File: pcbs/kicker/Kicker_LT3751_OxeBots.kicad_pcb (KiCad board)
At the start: 2 copper layers, 117.9 x 140 mm, 127 parts, among them J1 XT30PW-F, J2 12V, J3 3.3V, J4 I2C, J5 ST Link, J6 XT30PW-F, Q1 IRFB4227, Q2 BSS138, Q3 BSS138, Q4 FQPF20N60, SW1 SW_Push, T1 DCT15EFD-U44S003, U1 STM32G031F6Px, U2 LT3751, U3 TLV9002, U4 AQV454, U5 HCNR201, U6 HCPL-3120, U7 LM358

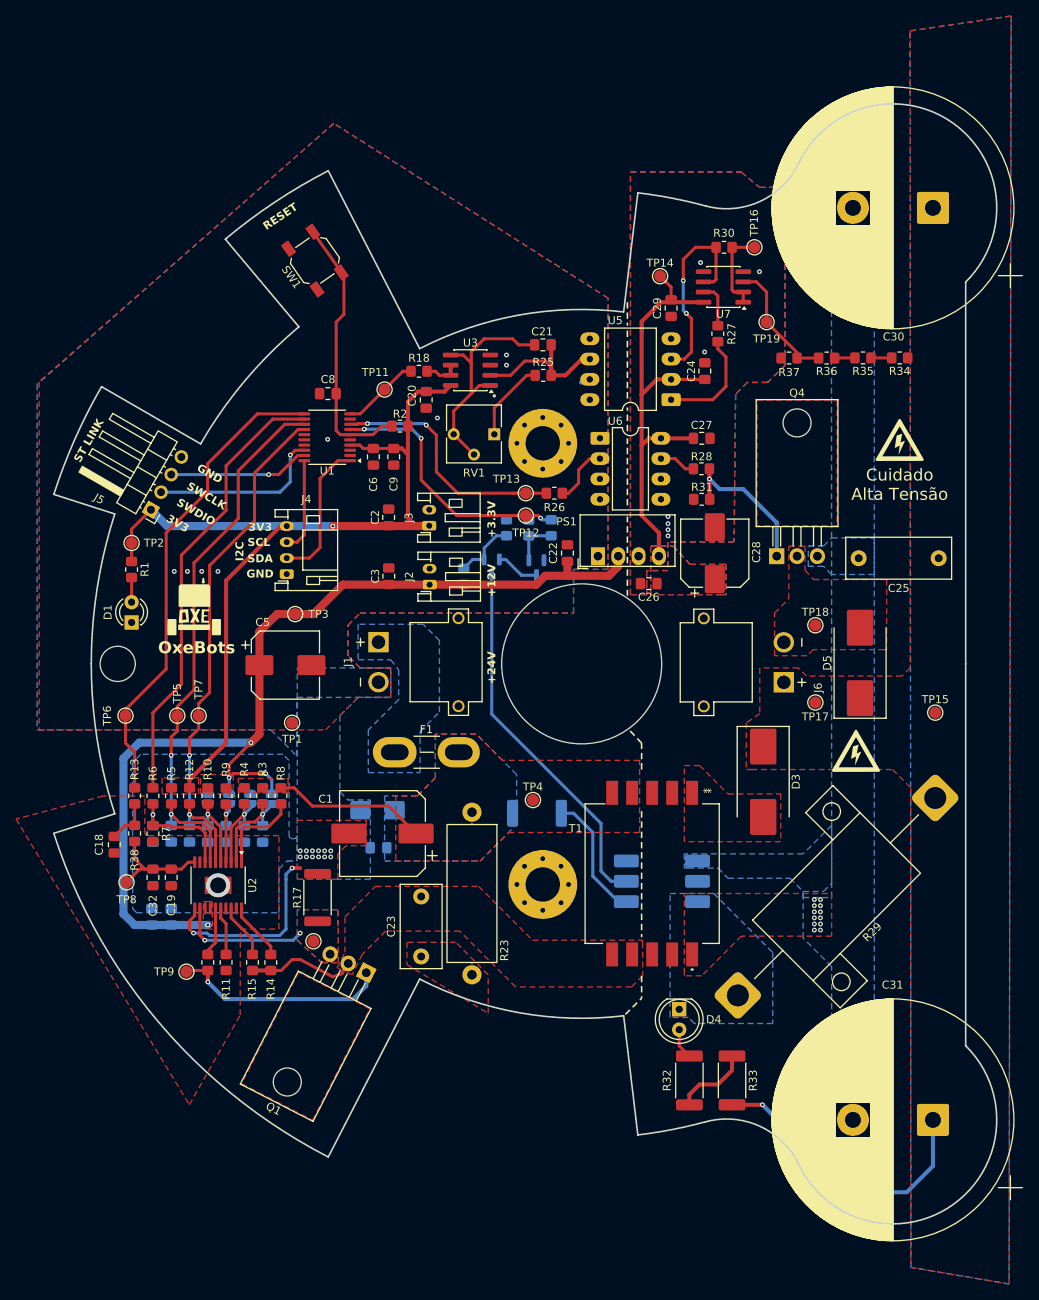
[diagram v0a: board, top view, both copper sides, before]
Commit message: Updated to IDC Connector
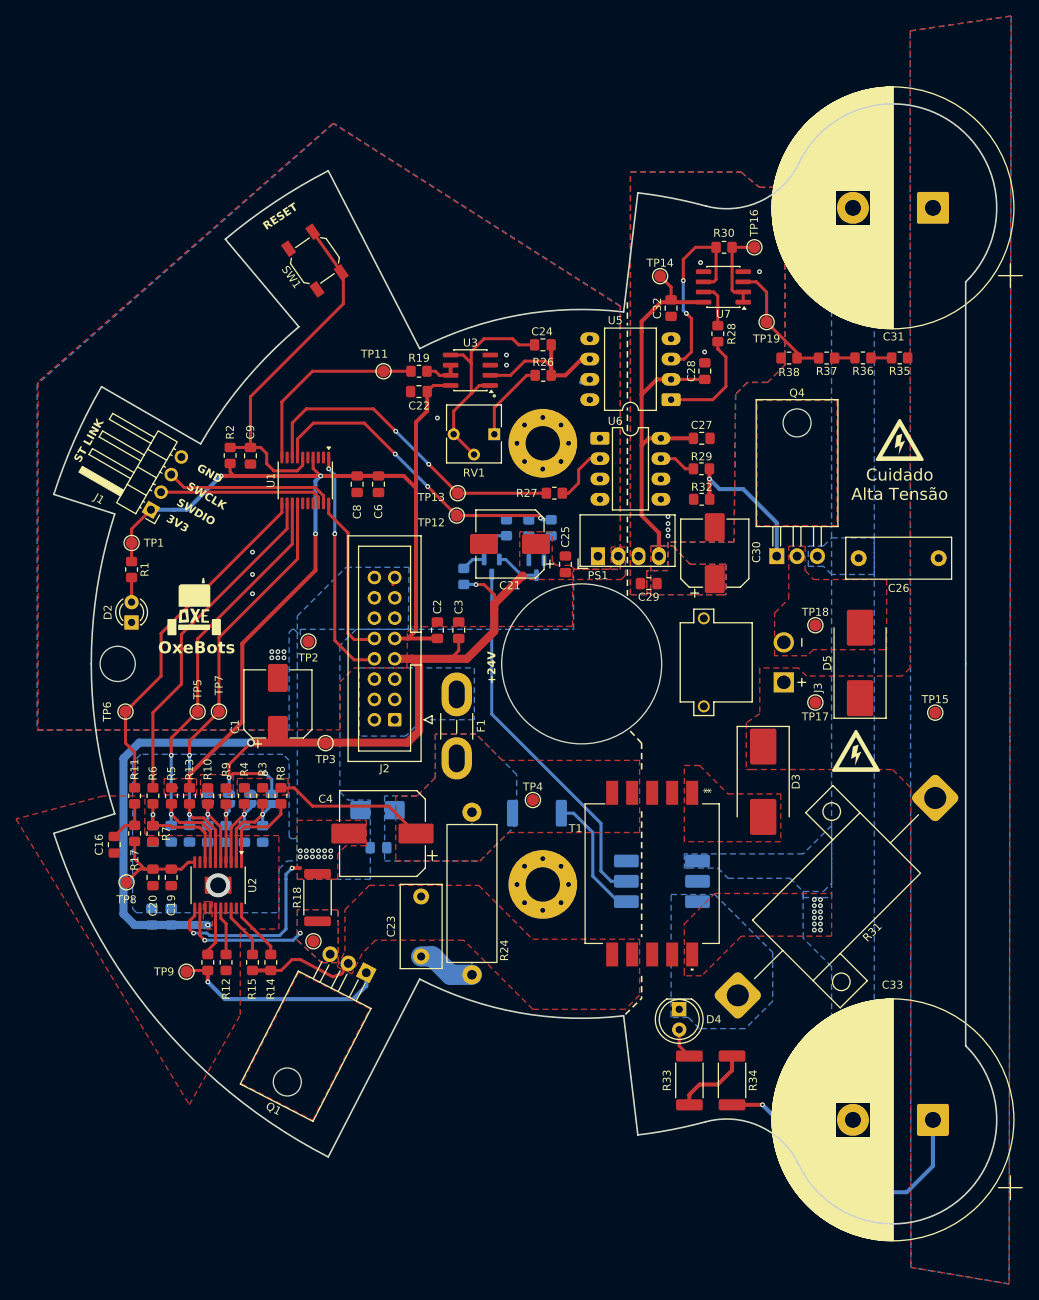
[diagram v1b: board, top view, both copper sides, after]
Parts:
- removed the J1 at (88.8, 101.5)
- removed the J3 at (85.2, 84.5)
- removed J4: I2C, Connector_JST:JST_PH_S4B-PH-K_1x04_P2.00mm_Horizontal
- added C21: 470uF, Capacitor_SMD:CP_Elec_8x10, F.Cu at (95.3, 86.7)
- J2: value 12V -> IDC_16_pin_Odd_Even; footprint Connector_JST:JST_PH_S2B-PH-K_1x02_P2.00mm_Horizontal -> Connector_IDC:IDC-Header_2x08_P2.54mm_Vertical
- moved R2 21.5 mm to (60.3, 75.7), turned to 90 degrees
- moved J2 17.4 mm to (80.9, 108.7), turned to 180 degrees
- moved TP3 16.6 mm to (72.2, 111.6)
- moved C2 15.4 mm to (86.2, 97.5)
- moved C9 12.4 mm to (62.8, 75.7), turned to -90 degrees
- moved C3 11.0 mm to (88.9, 97.5)
- moved F1 10.6 mm to (88.6, 105.5), turned to -90 degrees
- moved TP2 10.4 mm to (70.1, 98.9)
- moved TP12 8.64 mm to (88.6, 83.2)
- moved TP13 8.51 mm to (88.7, 80.4)
- moved U1 6.05 mm to (69.7, 78.8), turned to -90 degrees
- moved C1 4.94 mm to (66.3, 106.7), turned to 90 degrees
- moved C8 3.99 mm to (76.2, 79.3)
- moved C6 3.92 mm to (78.8, 79.3)
- moved TP7 2.59 mm to (58.9, 107.7)
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- renumbered C5 to C1, C13 to C11, C11 to C12, C12 to C13, C17 to C15, C18 to C16, C15 to C17, C16 to C18, C32 to C20, C20 to C22, C21 to C24, C22 to C25, C25 to C26, C24 to C28, C26 to C29, C28 to C30, C30 to C31, C29 to C32, C31 to C33, C1 to C4, C4 to C5, C9 to C6, C6 to C8, C8 to C9, D2 to D1, D1 to D2, J5 to J1, J6 to J3, R13 to R11, R11 to R12, R12 to R13, R38 to R17, R17 to R18, R18 to R19, R19 to R20, R20 to R21, R21 to R22, R22 to R23, R23 to R24, R24 to R25, R25 to R26, R26 to R27, R27 to R28, R28 to R29, R29 to R31, R31 to R32, R32 to R33, R33 to R34, R34 to R35, R35 to R36, R36 to R37, R37 to R38, TP2 to TP1, TP1 to TP2
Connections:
- net MCU_OUT_ENABLE renamed MCU_OUT_CHARGE
- F1 pad 1: Net-(F1-Pad1) -> +24V_INPUT
- J2 pad 1: +12V -> +24V_INPUT
- J2 pad 2: GND -> +24V_INPUT
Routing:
- net +3.3V: track 111.4 -> 134.4 mm, vias 1 -> 3
- net MCU_PWM_OUT_FB: track 59.9 -> 44.1 mm
- net MCU_ADC_IN_FB: track 9.82 -> 24.7 mm
- net MCU_OUT_CHARGE: track 56.2 -> 42.5 mm
- net +12V: track 137.7 -> 125.1 mm, vias 4 -> 5
- net LT3751_DONE: track 69.4 -> 57.5 mm
- net MCU_NRST: track 27.7 -> 39.5 mm
- net MCU_I2C_SDA: track 18.0 -> 29.0 mm, vias 0 -> 2
- net MCU_PWM_OUT_KICK: track 30.8 -> 41.2 mm
- net LT3751_FAULT: track 65.3 -> 55.2 mm
- net MCU_I2C_SCL: track 11.8 -> 20.7 mm
- net Net-(C23-Pad1): track 0.00 -> 7.30 mm
- net MCU_OUT_BLEEDER: track 34.8 -> 39.9 mm
- net MCU_STLINK_SWCLK: track 17.6 -> 21.3 mm, vias 1 -> 0
- net MCU_STLINK_SWDIO: track 22.0 -> 20.7 mm, vias 1 -> 0
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- added copper zone on B.Cu, net +24V_INPUT
- removed copper zone on F.Cu, net Net-(C23-Pad1)
- removed copper zone on B.Cu, net Net-(F1-Pad1)
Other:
- board text removed: "+12V"
- board text removed: "+3.3V"
- board text removed: "I2C"
- board text removed: "SCL"
- board text removed: "SDA"

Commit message: include gerber files
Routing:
- net GND: vias 25 -> 26

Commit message: added I2C pull-up resistors
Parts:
- added R39: 10k, Resistor_SMD:R_0805_2012Metric_Pad1.20x1.40mm_HandSolder, F.Cu at (72.0, 85.5)
- added R40: 10k, Resistor_SMD:R_0805_2012Metric_Pad1.20x1.40mm_HandSolder, F.Cu at (72.0, 88.9)
- moved C6 1.14 mm to (77.7, 79.3)
- moved C8 1.14 mm to (75.0, 79.3)
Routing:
- net MCU_I2C_SCL: track 20.7 -> 22.5 mm
- net GND: vias 26 -> 34

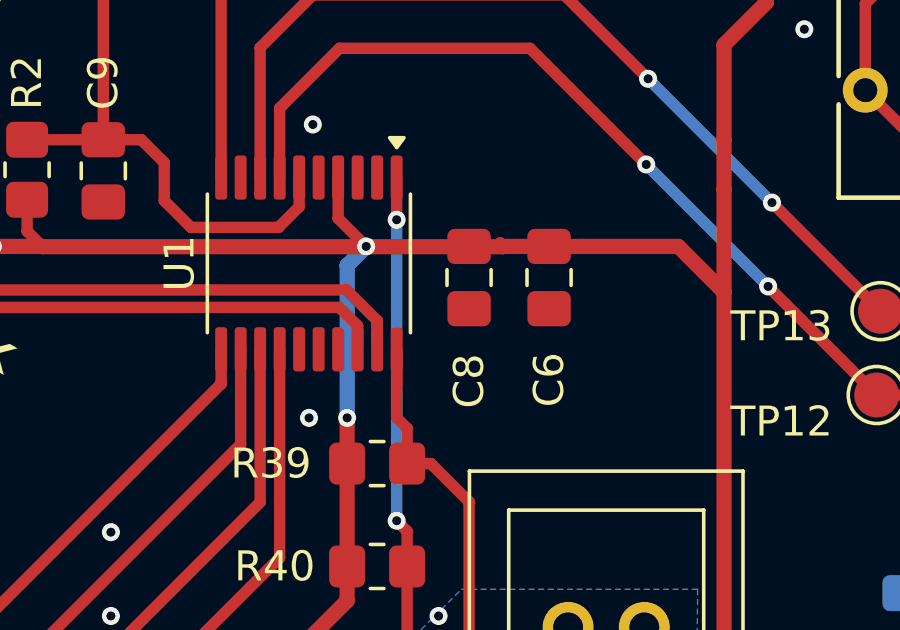
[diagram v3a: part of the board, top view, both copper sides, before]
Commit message: Fix warnings and add gnd debug pad
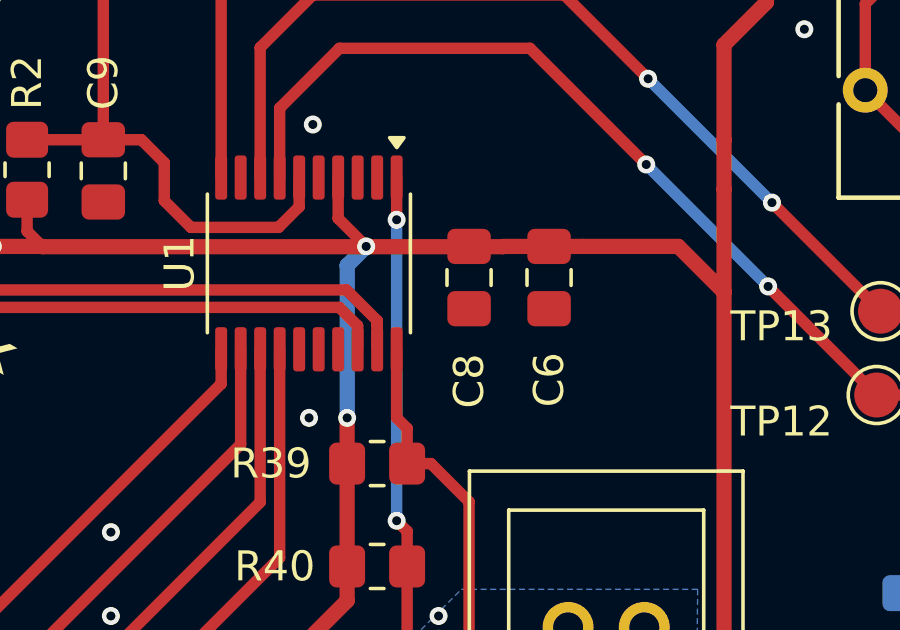
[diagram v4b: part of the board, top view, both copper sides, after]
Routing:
- net MCU_I2C_SCL: track 22.5 -> 21.2 mm
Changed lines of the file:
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@@
 		(net "Net-(Q1-D)")
+	)
+	(gr_circle
+		(center 70.319 50.292)
+		(end 74.319 50.292)
+		(stroke
+			(width 0.2)
+			(type solid)
+		)
+		(fill yes)
+		(layer "B.Mask")
 	)
 	(gr_line
@@
 		)
 	)
+	(gr_text "GND"
+		(at 72.351 42.291 90)
+		(layer "B.SilkS")
+		(effects
+			(font
+				(size 1 1)
+				(thickness 0.15)
+			)
+			(justify left bottom mirror)
+		)
+	)
 	(gr_text "Cuidado\nAlta Tensão"
 		(at 143.471 76.073 0)
@@
 	)
 	(segment
-		(start 76.161 78.2105)
-		(end 76.0555 78.105)
-		(width 0.381)
-		(layer "F.Cu")
-		(net "+3.3V")
-	)
-	(segment
 		(start 76.161 78.232)
 		(end 78.828 78.232)
@@
 		(width 0.381)
 		(layer "F.Cu")
-		(net "MCU_I2C_SCL")
-	)
-	(segment
-		(start 72.605 82.931)
-		(end 72.605 81.661)
-		(width 0.381)
-		(layer "F.Cu")

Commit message: Edit silkscreen and re-export files
- Export step file and gerbers
- Add pinout notes on silkscreen
- Add revision note and date
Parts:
- removed the G*** at (55.7, 95.0)
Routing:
- net GND: vias 34 -> 105
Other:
- board text added: "Notes:"
- board text removed: "OxeBots"
